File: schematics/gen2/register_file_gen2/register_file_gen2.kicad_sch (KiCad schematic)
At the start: 15 parts, among them J1 Conn_02x25_Counter_Clockwise, U1 74LS02, U3 74LS02

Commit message: implemented pcb for register file
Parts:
- removed C12: C, symbol Device:C
- removed J1: Conn_02x25_Counter_Clockwise, Connector_PinSocket_2.54mm:PinSocket_2x25_P2.54mm_Horizontal, symbol Connector_Generic:Conn_02x25_Counter_Clockwise
- removed U3: 74LS02, symbol 74xx:74LS02
- added BC1: BusConnector, Connector_PCBEdge:BUS_PCIexpress_x16, symbol cpu816symbols:BusConnector
- added C6: C, Capacitor_SMD:C_0805_2012Metric_Pad1.18x1.45mm_HandSolder, symbol Device:C
- added U2: 74LS02, Package_DIP:DIP-14_W7.62mm_Socket_LongPads, symbol 74xx:74LS02
- C1, C10, C2, C3, C4, C5: footprint (none) -> Capacitor_SMD:C_0805_2012Metric_Pad1.18x1.45mm_HandSolder
- U1: footprint (none) -> Package_DIP:DIP-14_W7.62mm_Socket_LongPads
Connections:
- net ~CLK is gone; now on net GND: U1.12, U1.3, U1.6, U1.9
- net D0: now also BC1.A51 (DATA0)
- net D1: now also BC1.A52 (DATA1)
- net D2: now also BC1.A53 (DATA2)
- net D3: now also BC1.A54 (DATA3)
- net D4: now also BC1.A55 (DATA4)
- net D5: now also BC1.A56 (DATA5)
- net D6: now also BC1.A57 (DATA6)
- net D7: now also BC1.A58 (DATA7)
- net GND: now also BC1.A12 (GND), BC1.A13 (GND), BC1.A23 (GND), BC1.A32 (GND), BC1.A41 (GND), BC1.A50 (GND), BC1.A59 (GND), BC1.A63 (GND), BC1.A64 (GND), BC1.A65 (GND), BC1.A66 (GND), BC1.A70 (GND), BC1.A71 (GND), BC1.A72 (GND), BC1.A73 (GND), BC1.A74 (GND), BC1.A75 (GND), BC1.A76 (GND), BC1.B12 (GND), BC1.B13 (GND), BC1.B23 (GND), BC1.B32 (GND), BC1.B41 (GND), BC1.B50 (GND), BC1.B59 (GND), BC1.B62 (GND), BC1.B63 (GND), BC1.B64 (GND), BC1.B65 (GND), BC1.B66 (GND), BC1.B67 (GND), BC1.B68 (GND), BC1.B69 (GND), BC1.B70 (GND), BC1.B71 (GND), BC1.B72 (GND), BC1.B73 (~{CLK}), BC1.B75 (GND), BC1.B76 (GND), C6.2, U2.3, U2.7 (GND)
- net VCC: now also BC1.A1 (VCC), BC1.A2 (VCC), BC1.A3 (VCC), BC1.A4 (VCC), BC1.A5 (VCC), BC1.B1 (VCC), BC1.B2 (VCC), BC1.B3 (VCC), BC1.B4 (VCC), BC1.B5 (VCC), C6.1, U2.14 (VCC)
- net at R1.11 (Cp): now also U2.1
- net ~{LOAD_R0}: no longer names the net of U1.2
- net ~{LOAD_R0}: now also BC1.A27 (~{LZH})
- net ~{LOAD_R2}: no longer names the net of U1.8
- net ~{LOAD_R2}: now also BC1.A25 (~{LYH})
- net ~{LOAD_R3}: no longer names the net of U1.11
- net ~{LOAD_R3}: now also BC1.A24 (~{LYL})
- net ~{LOAD_R4}: no longer names the net of U1.5
- net ~{LOAD_R4}: now also BC1.A22 (~{LXH})
- net ~{OUT_R0}: no longer names the net of R0.1 (OE)
- net ~{OUT_R0}: now also BC1.B27 (~{RZH})
- net ~{OUT_R1}: no longer names the net of R1.1 (OE)
- net ~{OUT_R1}: now also BC1.B26 (~{RZL})
- net ~{OUT_R2}: no longer names the net of R2.1 (OE)
- net ~{OUT_R2}: now also BC1.B25 (~{RYH})
- net ~{OUT_R3}: no longer names the net of R3.1 (OE)
- net ~{OUT_R3}: now also BC1.B24 (~{RYL})
- net ~{OUT_R4}: no longer names the net of R4.1 (OE)
- net ~{OUT_R4}: now also BC1.B22 (~{RXH})
- new net: BC1.A26 (~{LZL}), U2.2
- no-connect marks 26 -> 82
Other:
- moved on the sheet: C1, C10, C2, C3, C4, C5, R0, R1, R2, R3, R4, U1A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

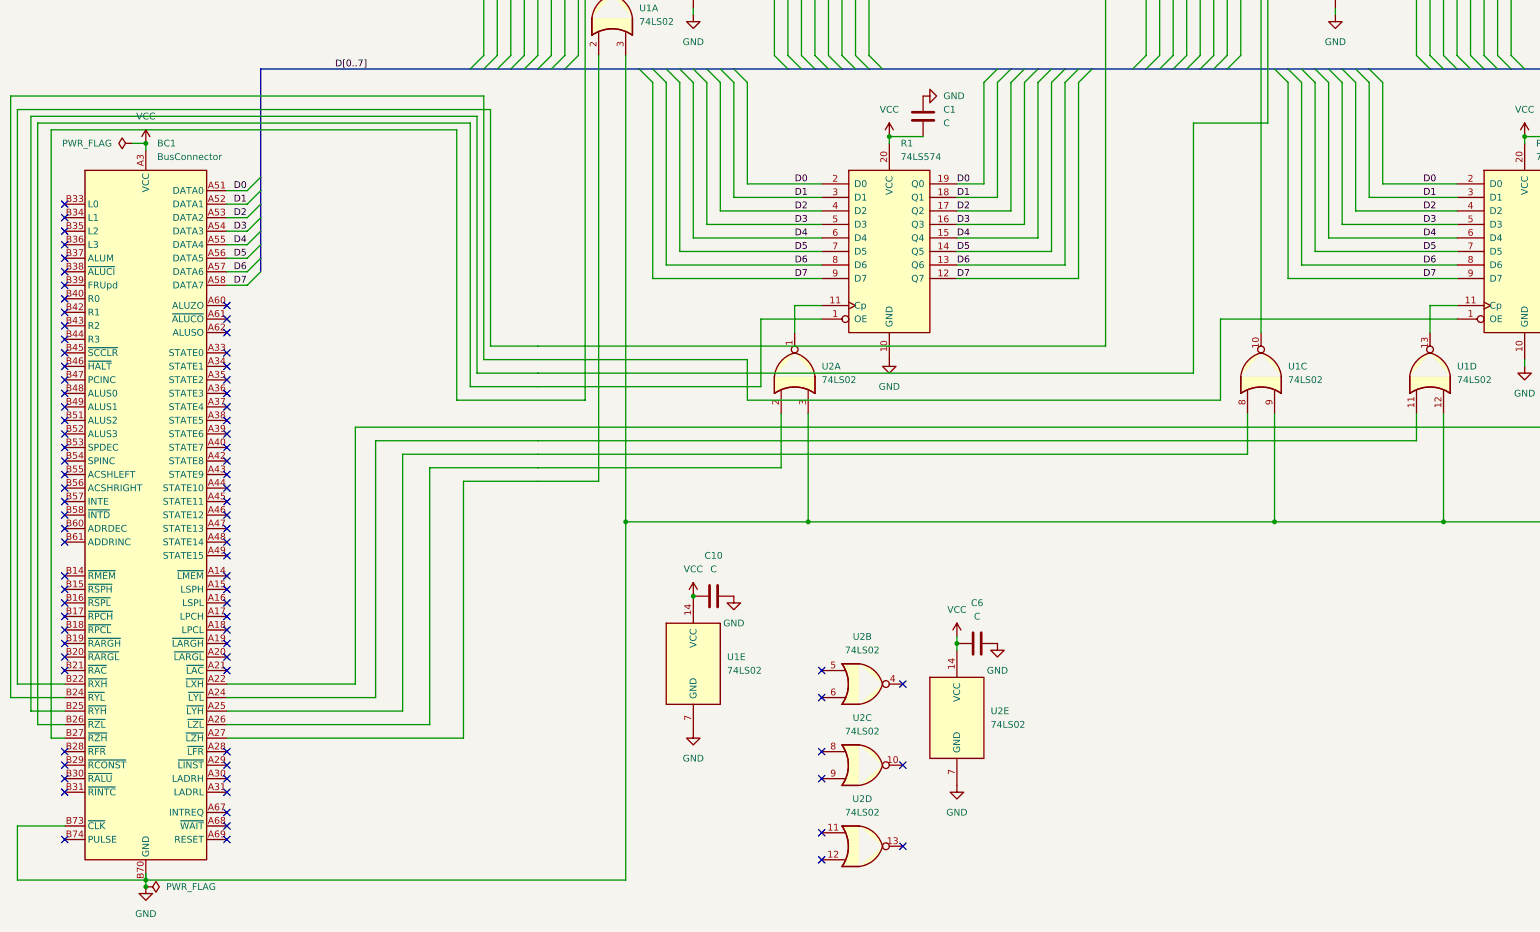
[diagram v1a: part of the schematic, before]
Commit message: fix(register file): added pull up resistor fixed schematic, changed capacitors
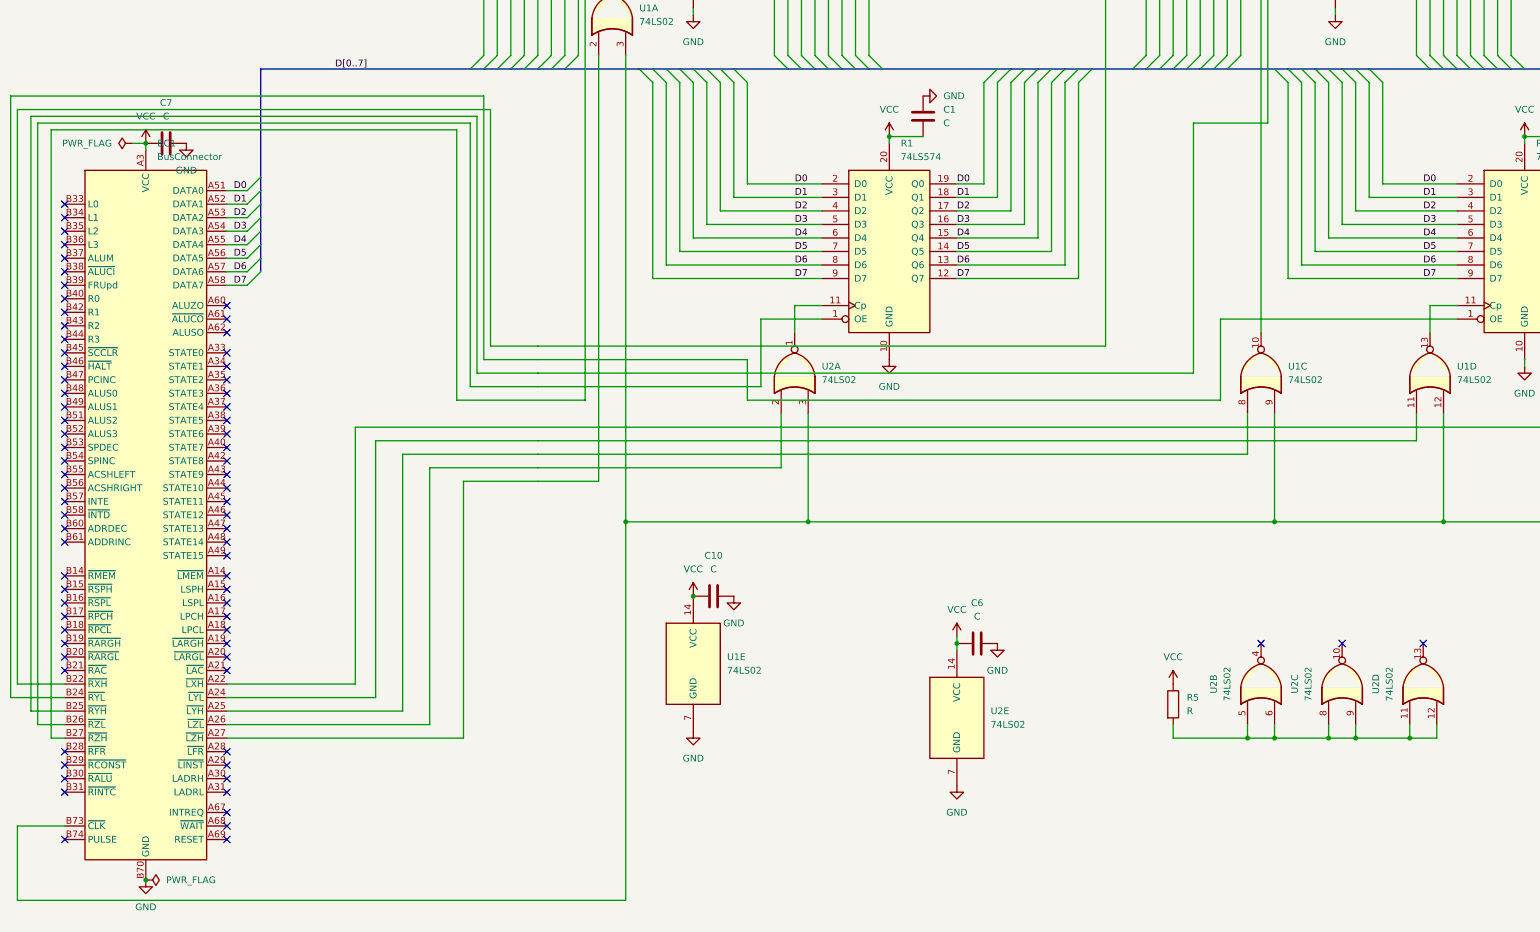
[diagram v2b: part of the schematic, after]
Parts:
- added C7: C, Capacitor_THT:C_Radial_D6.3mm_H5.0mm_P2.50mm, symbol Device:C
- added R5: R, Resistor_THT:R_Axial_DIN0207_L6.3mm_D2.5mm_P7.62mm_Horizontal, symbol Device:R
- C1, C10, C2, C3, C4, C5, C6: footprint Capacitor_SMD:C_0805_2012Metric_Pad1.18x1.45mm_HandSolder -> Capacitor_THT:C_Disc_D5.0mm_W2.5mm_P5.00mm
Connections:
- net GND: now also C7.2; no longer BC1.B73 (~{CLK}), U1.12, U1.3, U1.6, U1.9, U2.3
- net VCC: now also C7.1, R5.1
- net at U2.8: now also U2.11, U2.12, U2.5, U2.6, U2.9, R5.2
- new net: BC1.B73 (~{CLK}), U1.12, U1.3, U1.6, U1.9, U2.3
- no-connect marks 82 -> 76
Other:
- moved on the sheet: U2B, U2C, U2D
